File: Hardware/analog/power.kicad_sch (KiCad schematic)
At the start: 26 parts, among them U401 ICL7660, U402 MCP1804x-C002xMB, U403 MCP1703AT-5002E/DB, U404 XC6203E33

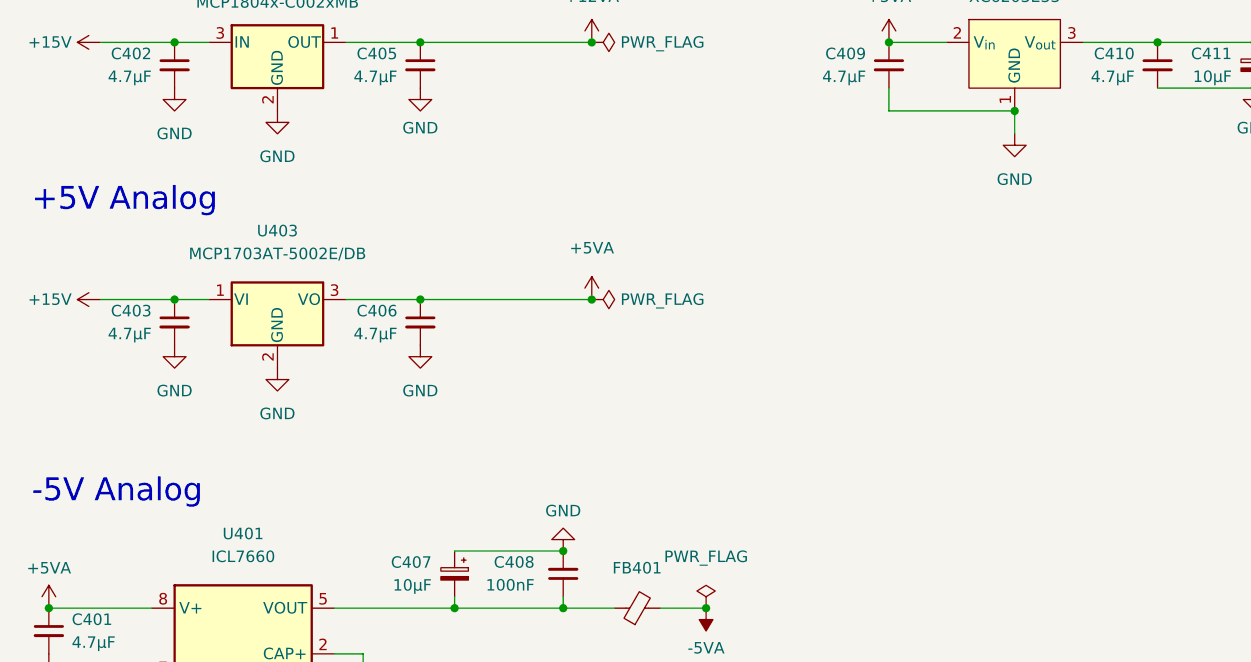
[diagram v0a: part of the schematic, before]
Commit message: Added ADC/DAC section
- Imported the schematic for the analog DAC/ADC section, as well as the
  Vref generator and clock generator for the ADC
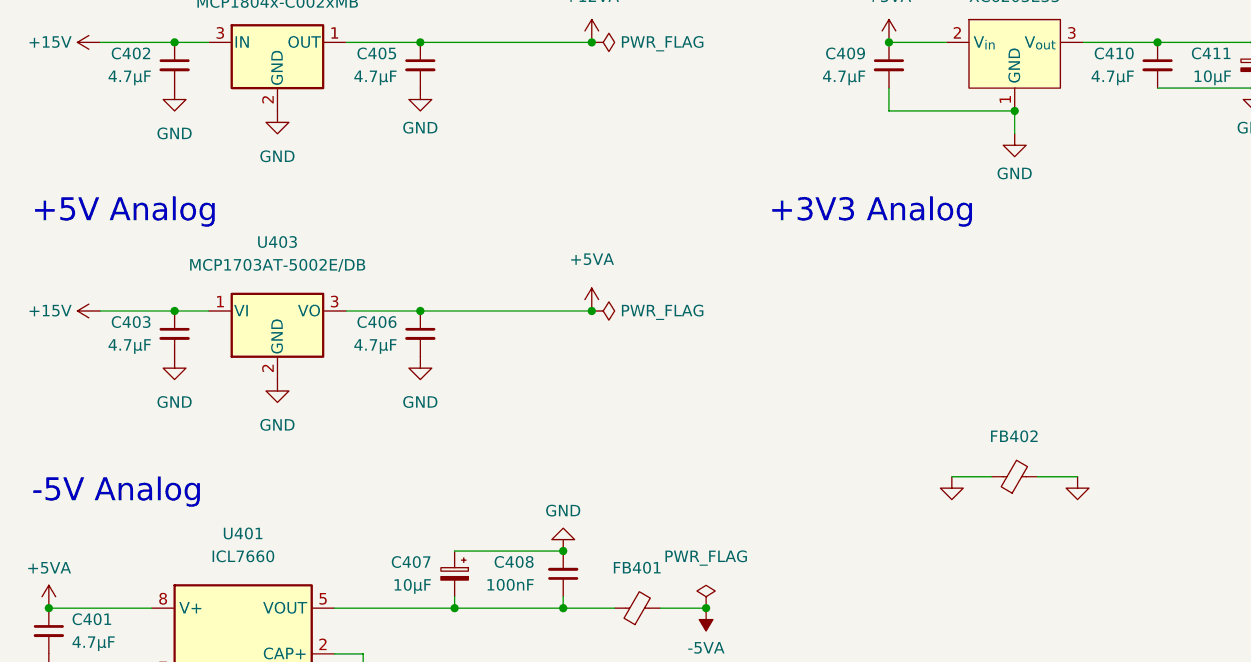
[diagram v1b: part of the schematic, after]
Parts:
- added FB402: FerriteBead_Small, Inductor_SMD:L_0805_2012Metric_Pad1.05x1.20mm_HandSolder, symbol Device:FerriteBead_Small
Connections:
- net GND: now also FB402.1
- new net GNDA: FB402.2
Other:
- note added: "+3V3 Analog"
- moved on the sheet: C403, C406, U403

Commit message: Add ADC aliasing filters
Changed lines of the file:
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@@
       (effects (font (size 1.27 1.27)) hide)
     )
-    (property "Value" "" (id 1) (at 121.285 85.09 0))
+    (property "Value" "GND" (id 1) (at 121.285 85.09 0))
     (property "Footprint" "" (id 2) (at 121.285 80.01 0)
       (effects (font (size 1.27 1.27)) hide)
@@
       (effects (font (size 1.27 1.27)) hide)
     )
-    (property "Value" "" (id 1) (at 135.255 85.09 0))
+    (property "Value" "GNDA" (id 1) (at 135.255 85.09 0))
     (property "Footprint" "" (id 2) (at 135.255 80.01 0)
       (effects (font (size 1.27 1.27)) hide)

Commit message: Start work on analog island
- This is the part with the ADC/DAC/reference which has its own analog
  ground and voltage, generated from +5V
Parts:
- added C412: 10µF, Capacitor_Tantalum_SMD:CP_EIA-3216-18_Kemet-A_Pad1.58x1.35mm_HandSolder, symbol Device:C_Polarized_Small
- added C413, C414: 4.7µF, Capacitor_SMD:C_0805_2012Metric_Pad1.18x1.45mm_HandSolder, symbol Device:C_Small
- added D406: Green, LED_SMD:LED_0805_2012Metric_Pad1.15x1.40mm_HandSolder, symbol Device:LED_Small
- added R406: 1k, Resistor_SMD:R_0805_2012Metric_Pad1.20x1.40mm_HandSolder, symbol Device:R_Small
- added U405: LP5907MFX-3.3, Package_TO_SOT_SMD:SOT-23-5, symbol Regulator_Linear:LP5907MFX-3.3
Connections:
- net +5VA: now also C412.1, C413.1, U405.1 (IN), U405.3 (EN)
- net GND: now also C412.2, C413.2
- net GNDA: now also C414.2, D406.1 (K), U405.2 (GND)
- new net: D406.2 (A), R406.2
- new net +3V3A: C414.1, R406.1, U405.5 (OUT)
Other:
- note added: "This is to go near the ADC/DAC analog island"
- moved on the sheet: C409, C410, C411, FB402, U404

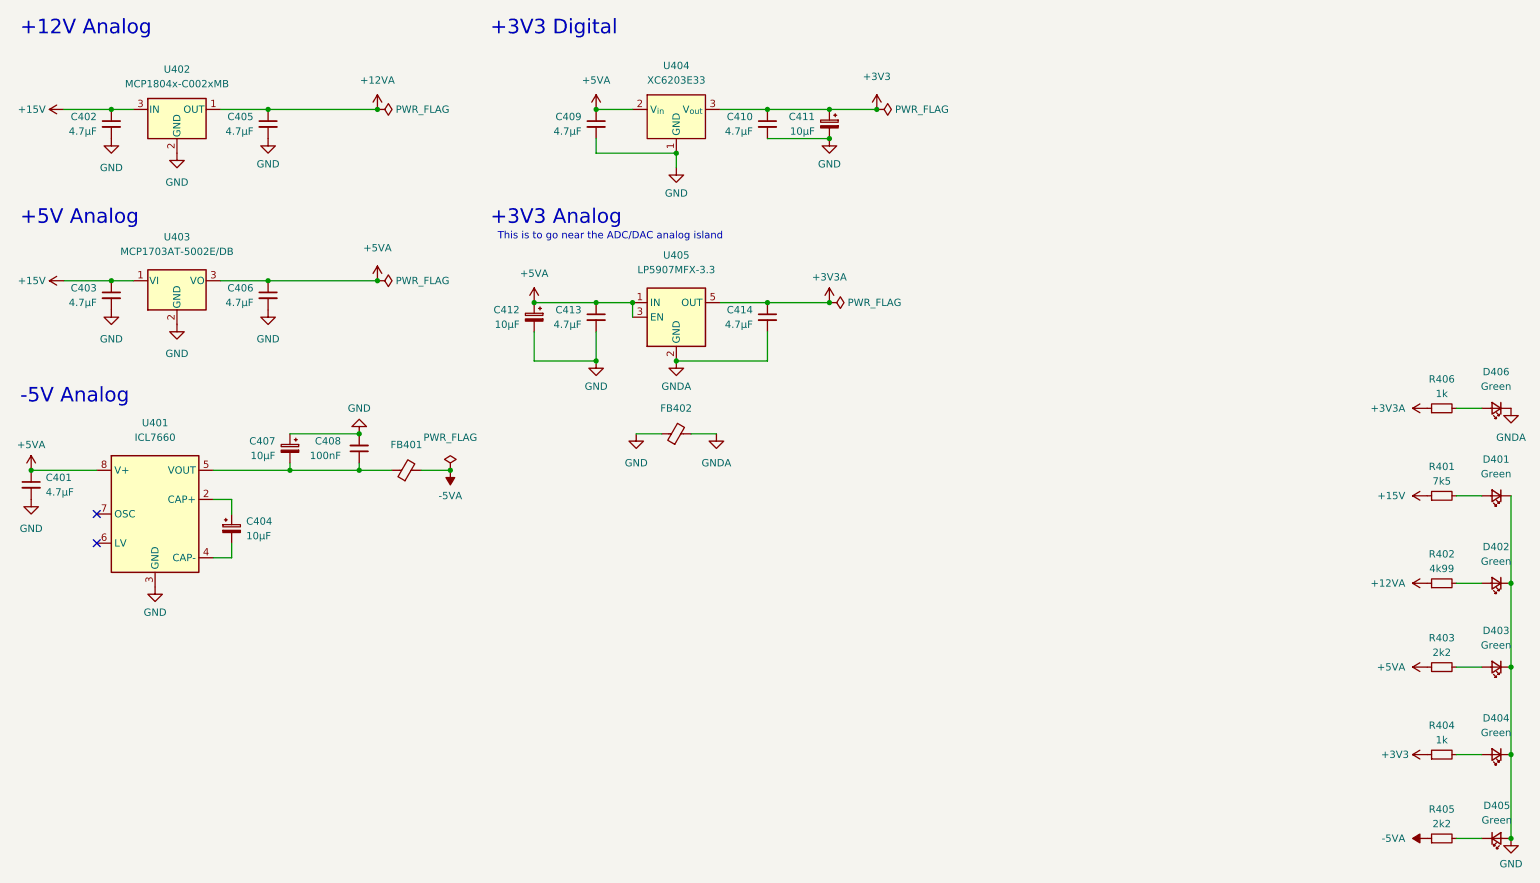
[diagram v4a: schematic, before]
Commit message: Added more decoupling for reference
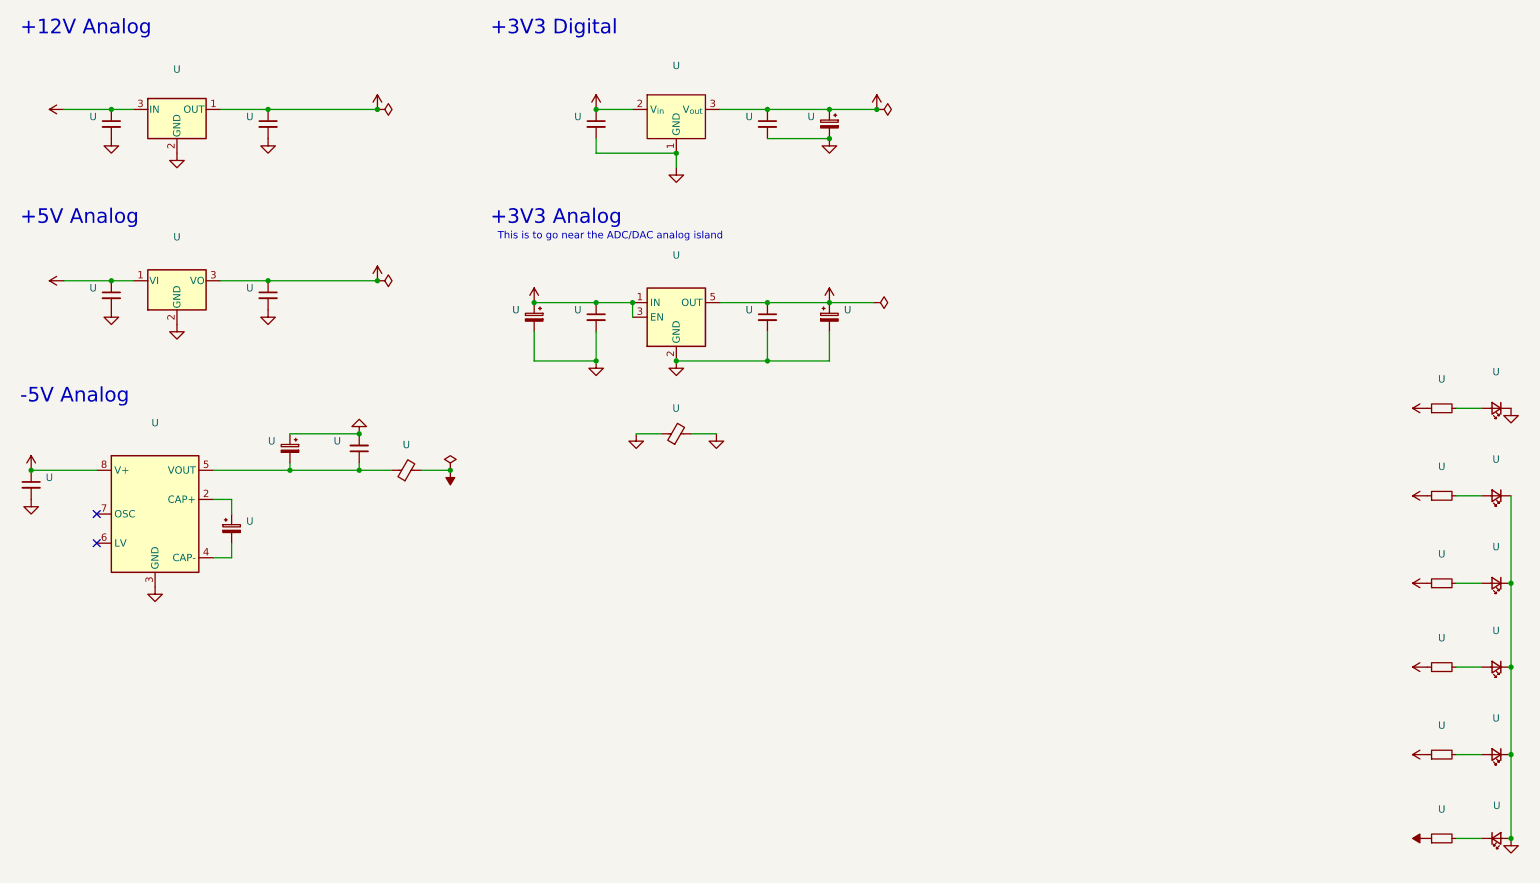
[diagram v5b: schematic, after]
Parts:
- added U: (no value), symbol Device:C_Polarized_Small
- U: renamed from C410; value 4.7µF -> (none); footprint Capacitor_SMD:C_0805_2012Metric_Pad1.18x1.45mm_HandSolder -> (none)
- U: renamed from R404; value 1k -> (none); footprint Resistor_SMD:R_0805_2012Metric_Pad1.20x1.40mm_HandSolder -> (none)
- U: renamed from C414; value 4.7µF -> (none); footprint Capacitor_SMD:C_0805_2012Metric_Pad1.18x1.45mm_HandSolder -> (none)
- U: renamed from D405; value Green -> (none); footprint LED_SMD:LED_0805_2012Metric_Pad1.15x1.40mm_HandSolder -> (none)
- U: renamed from FB402; value FerriteBead_Small -> (none); footprint Inductor_SMD:L_0805_2012Metric_Pad1.05x1.20mm_HandSolder -> (none)
- U: renamed from C404; value 10µF -> (none); footprint Capacitor_Tantalum_SMD:CP_EIA-3216-18_Kemet-A_Pad1.58x1.35mm_HandSolder -> (none)
- U: renamed from R403; value 2k2 -> (none); footprint Resistor_SMD:R_0805_2012Metric_Pad1.20x1.40mm_HandSolder -> (none)
- U: renamed from D404; value Green -> (none); footprint LED_SMD:LED_0805_2012Metric_Pad1.15x1.40mm_HandSolder -> (none)
- U: renamed from R402; value 4k99 -> (none); footprint Resistor_SMD:R_0805_2012Metric_Pad1.20x1.40mm_HandSolder -> (none)
- U: renamed from U404; value XC6203E33 -> (none); footprint Package_TO_SOT_SMD:SOT-223 -> (none)
- U: renamed from C401; value 4.7µF -> (none); footprint Capacitor_SMD:C_0805_2012Metric_Pad1.18x1.45mm_HandSolder -> (none)
- U: renamed from D406; value Green -> (none); footprint LED_SMD:LED_0805_2012Metric_Pad1.15x1.40mm_HandSolder -> (none)
- U: renamed from C411; value 10µF -> (none); footprint Capacitor_Tantalum_SMD:CP_EIA-3216-18_Kemet-A_Pad1.58x1.35mm_HandSolder -> (none)
- U: renamed from FB401; value FerriteBead_Small -> (none); footprint Inductor_SMD:L_0805_2012Metric_Pad1.05x1.20mm_HandSolder -> (none)
- U: renamed from C407; value 10µF -> (none); footprint Capacitor_Tantalum_SMD:CP_EIA-3216-18_Kemet-A_Pad1.58x1.35mm_HandSolder -> (none)
- U: renamed from D401; value Green -> (none); footprint LED_SMD:LED_0805_2012Metric_Pad1.15x1.40mm_HandSolder -> (none)
- U: renamed from R401; value 7k5 -> (none); footprint Resistor_SMD:R_0805_2012Metric_Pad1.20x1.40mm_HandSolder -> (none)
- U: renamed from C403; value 4.7µF -> (none); footprint Capacitor_SMD:C_0805_2012Metric_Pad1.18x1.45mm_HandSolder -> (none)
- U: renamed from C408; value 100nF -> (none); footprint Capacitor_SMD:C_0805_2012Metric_Pad1.18x1.45mm_HandSolder -> (none)
- U: renamed from C406; value 4.7µF -> (none); footprint Capacitor_SMD:C_0805_2012Metric_Pad1.18x1.45mm_HandSolder -> (none)
- U: renamed from R405; value 2k2 -> (none); footprint Resistor_SMD:R_0805_2012Metric_Pad1.20x1.40mm_HandSolder -> (none)
- U: renamed from C409; value 4.7µF -> (none); footprint Capacitor_SMD:C_0805_2012Metric_Pad1.18x1.45mm_HandSolder -> (none)
- U: renamed from U401; value ICL7660 -> (none); footprint Package_SO:SOIC-8_3.9x4.9mm_P1.27mm -> (none)
- U: renamed from C405; value 4.7µF -> (none); footprint Capacitor_SMD:C_0805_2012Metric_Pad1.18x1.45mm_HandSolder -> (none)
- U: renamed from D403; value Green -> (none); footprint LED_SMD:LED_0805_2012Metric_Pad1.15x1.40mm_HandSolder -> (none)
- U: renamed from U403; value MCP1703AT-5002E/DB -> (none); footprint Package_TO_SOT_SMD:SOT-223-3_TabPin2 -> (none)
- U: renamed from C413; value 4.7µF -> (none); footprint Capacitor_SMD:C_0805_2012Metric_Pad1.18x1.45mm_HandSolder -> (none)
- U: renamed from U402; value MCP1804x-C002xMB -> (none); footprint Package_TO_SOT_SMD:SOT-89-3 -> (none)
- U: renamed from C412; value 10µF -> (none); footprint Capacitor_Tantalum_SMD:CP_EIA-3216-18_Kemet-A_Pad1.58x1.35mm_HandSolder -> (none)
- U: renamed from R406; value 1k -> (none); footprint Resistor_SMD:R_0805_2012Metric_Pad1.20x1.40mm_HandSolder -> (none)
- U: renamed from C402; value 4.7µF -> (none); footprint Capacitor_SMD:C_0805_2012Metric_Pad1.18x1.45mm_HandSolder -> (none)
- U: renamed from U405; value LP5907MFX-3.3 -> (none); footprint Package_TO_SOT_SMD:SOT-23-5 -> (none)
- U: renamed from D402; value Green -> (none); footprint LED_SMD:LED_0805_2012Metric_Pad1.15x1.40mm_HandSolder -> (none)
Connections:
- net +3V3A: now also U.1
- net GNDA: now also U.2

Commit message: Analog board layout
- Started work on adding the voltage sense circuitry, including the
  selector relay, IO expander to drive the relay, and the second ADC to
  convert the voltage values

- Changed the layout of analog board to better take advantage of
  available space

- Minor changes to front panel layout for aesthetics
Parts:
- U: MPN CL21A475KAQNNNF -> (none)
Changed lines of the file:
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@@
       (effects (font (size 1.27 1.27)) hide)
     )
-    (property "MPN" "CL21A475KAQNNNF" (id 4) (at 149.225 67.945 0)
+    (property "MPN" "" (id 4) (at 149.225 67.945 0)
       (effects (font (size 1.27 1.27)) hide)
     )
@@
       (effects (font (size 1.27 1.27)) hide)
     )
-    (property "MPN" "CL21A475KAQNNNF" (id 4) (at 20.955 97.155 0)
+    (property "MPN" "" (id 4) (at 20.955 97.155 0)
       (effects (font (size 1.27 1.27)) hide)
     )
@@
       (effects (font (size 1.27 1.27)) hide)
     )
-    (property "MPN" "CL21A475KAQNNNF" (id 4) (at 119.38 67.945 0)
-      (effects (font (size 1.27 1.27)) hide)
-    )
+    (property "MPN" "" (id 4) (at 119.38 67.945 0)
+      (effects (font (size 1.27 1.27)) hide)
+    )

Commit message: Mostly finished up analog load board
- Finished routing most signals

- Connected relay drive to bonus I2C GPIO controller, and routed the
  rest of the voltage sense stuff

- Routed the reset signal to the DAC, so that when the board is reset,
  the current output will be reset to zero as well without processor
  intervention

- Replaced most passives with 0603/1608 size
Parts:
- U: MPN CL21A475KAQNNNF -> (none)
- U: MPN CR0805-JW-102ELF -> (none)
- U: MPN RMC1/10-222JTP -> (none)
- U: MPN CR0805-FX-4991ELF -> (none)
- U: MPN WR08X752 JTL -> (none)
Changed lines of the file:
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@@
       (effects (font (size 1.27 1.27)) hide)
     )
-    (property "MPN" "CL21A475KAQNNNF" (id 4) (at 149.225 34.29 0)
+    (property "MPN" "" (id 4) (at 149.225 34.29 0)
       (effects (font (size 1.27 1.27)) hide)
     )
@@
       (effects (font (size 1.27 1.27)) hide)
     )
-    (property "MPN" "CR0805-JW-102ELF" (id 4) (at 266.7 144.145 90)
+    (property "MPN" "" (id 4) (at 266.7 144.145 90)
       (effects (font (size 1.27 1.27)) hide)
     )
@@
       (effects (font (size 1.27 1.27)) hide)
     )
-    (property "MPN" "RMC1/10-222JTP" (id 4) (at 266.7 128.905 90)
+    (property "MPN" "" (id 4) (at 266.7 128.905 90)
       (effects (font (size 1.27 1.27)) hide)
     )
@@
       (effects (font (size 1.27 1.27)) hide)
     )
-    (property "MPN" "CR0805-FX-4991ELF" (id 4) (at 266.7 114.3 90)
+    (property "MPN" "" (id 4) (at 266.7 114.3 90)
       (effects (font (size 1.27 1.27)) hide)
     )
@@
       (effects (font (size 1.27 1.27)) hide)
     )
-    (property "MPN" "WR08X752 JTL" (id 4) (at 266.7 99.06 90)
+    (property "MPN" "" (id 4) (at 266.7 99.06 90)
       (effects (font (size 1.27 1.27)) hide)
     )
@@
       (effects (font (size 1.27 1.27)) hide)
     )
-    (property "MPN" "CL21A475KAQNNNF" (id 4) (at 34.925 64.135 0)
+    (property "MPN" "" (id 4) (at 34.925 64.135 0)
       (effects (font (size 1.27 1.27)) hide)
     )
@@
       (effects (font (size 1.27 1.27)) hide)
     )
-    (property "MPN" "CL21A475KAQNNNF" (id 4) (at 62.23 64.135 0)
+    (property "MPN" "" (id 4) (at 62.23 64.135 0)
       (effects (font (size 1.27 1.27)) hide)
     )
@@
       (effects (font (size 1.27 1.27)) hide)
     )
-    (property "MPN" "RMC1/10-222JTP" (id 4) (at 266.7 158.75 90)
+    (property "MPN" "" (id 4) (at 266.7 158.75 90)
       (effects (font (size 1.27 1.27)) hide)
     )
@@
       (effects (font (size 1.27 1.27)) hide)
     )
-    (property "MPN" "CL21A475KAQNNNF" (id 4) (at 119.38 34.29 0)
+    (property "MPN" "" (id 4) (at 119.38 34.29 0)
       (effects (font (size 1.27 1.27)) hide)
     )
@@
       (effects (font (size 1.27 1.27)) hide)
     )
-    (property "MPN" "CL21A475KAQNNNF" (id 4) (at 62.23 34.29 0)
+    (property "MPN" "" (id 4) (at 62.23 34.29 0)
       (effects (font (size 1.27 1.27)) hide)
     )
@@
       (effects (font (size 1.27 1.27)) hide)
     )
-    (property "MPN" "CR0805-JW-102ELF" (id 4) (at 266.7 83.82 90)
+    (property "MPN" "" (id 4) (at 266.7 83.82 90)
       (effects (font (size 1.27 1.27)) hide)
     )
@@
       (effects (font (size 1.27 1.27)) hide)
     )
-    (property "MPN" "CL21A475KAQNNNF" (id 4) (at 34.925 34.29 0)
-      (effects (font (size 1.27 1.27)) hide)
-    )
+    (property "MPN" "" (id 4) (at 34.925 34.29 0)
+      (effects (font (size 1.27 1.27)) hide)
+    )
